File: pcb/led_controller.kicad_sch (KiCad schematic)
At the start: 38 parts, among them IC1 IS31FL3254-QFLS4-TR

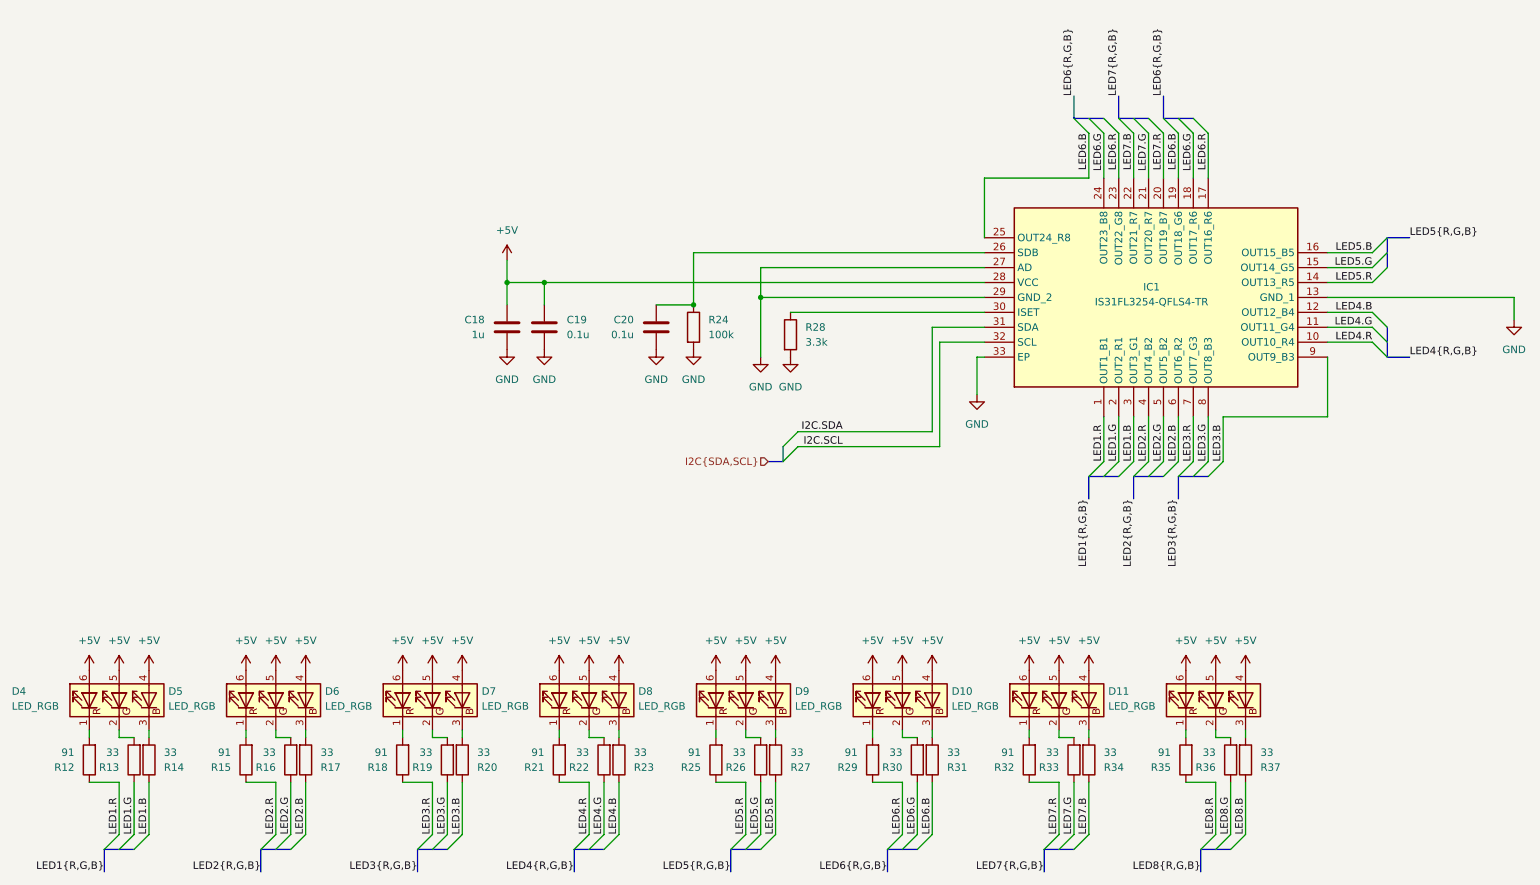
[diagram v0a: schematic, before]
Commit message: redraw led controller ic symbol
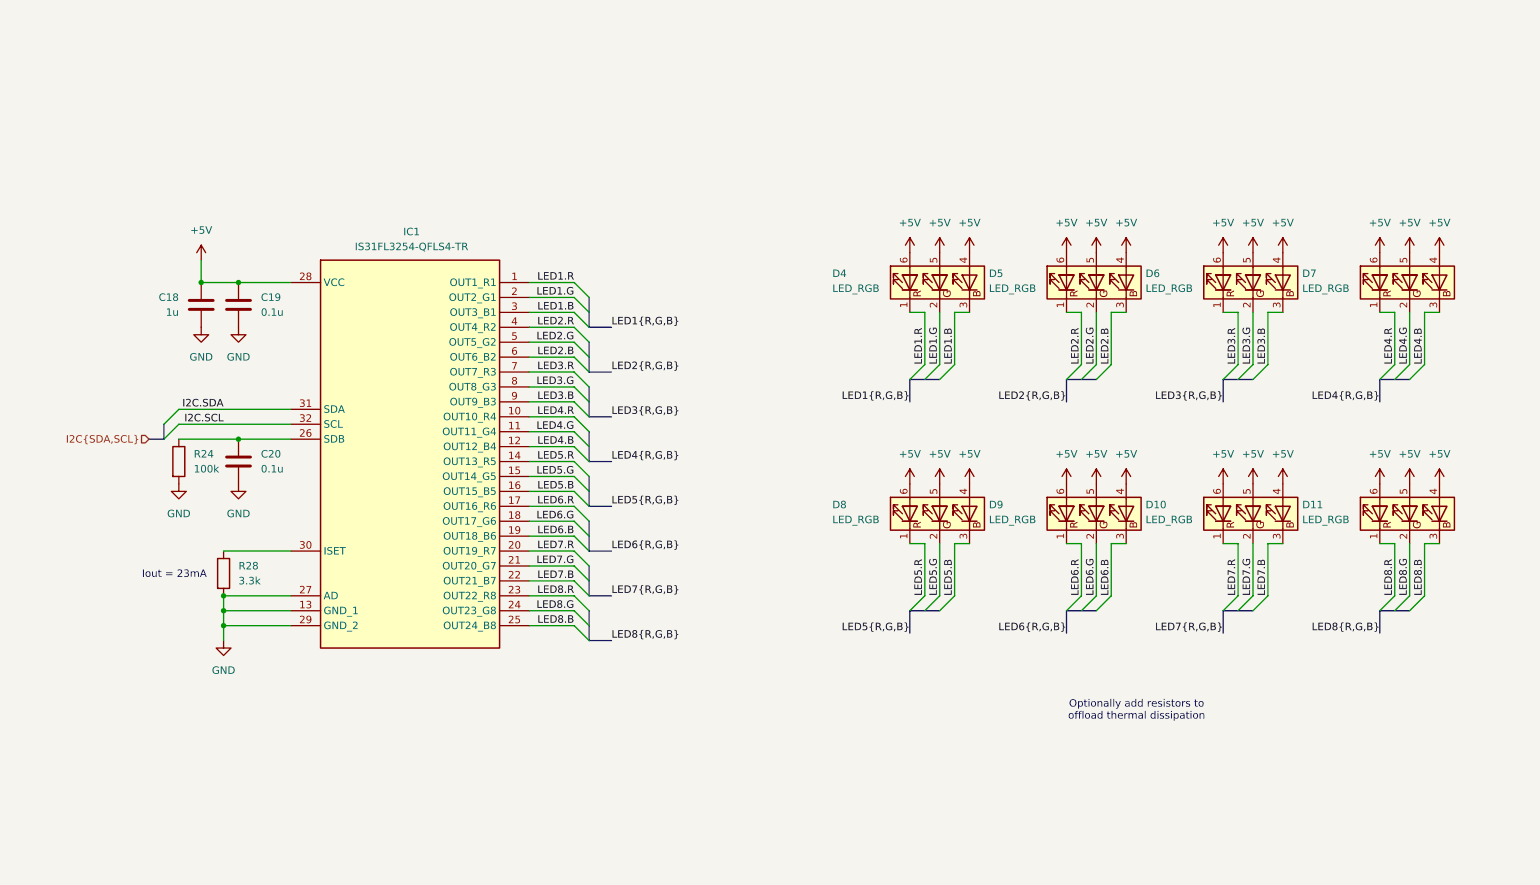
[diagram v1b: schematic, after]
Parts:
- removed R12, R15, R18, R21, R25, R29, R32, R35: 91, Resistor_SMD:R_0402_1005Metric, symbol Device:R
- removed R13, R14, R16, R17, R19, R20, R22, R23, R26, R27, R30, R31, R33, R34, R36, R37: 33, Resistor_SMD:R_0402_1005Metric, symbol Device:R
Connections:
- net GND: no longer IC1.33 (EP)
- net LED1.B: now also D4.3 (BK)
- net LED1.G: now also D4.2 (GK)
- net LED1.R: now also D4.1 (RK)
- net LED2.B: now also D5.3 (BK)
- net LED2.G: now also D5.2 (GK)
- net LED2.R: now also D5.1 (RK)
- net LED3.B: now also D6.3 (BK)
- net LED3.G: now also D6.2 (GK)
- net LED3.R: now also D6.1 (RK)
- net LED4.B: now also D7.3 (BK)
- net LED4.G: now also D7.2 (GK)
- net LED4.R: now also D7.1 (RK)
- net LED5.B: now also D8.3 (BK)
- net LED5.G: now also D8.2 (GK)
- net LED5.R: now also D8.1 (RK)
- net LED6.B: now also D9.3 (BK); no longer IC1.25 (OUT24_R8)
- net LED6.G: now also D9.2 (GK); no longer IC1.24 (OUT23_B8)
- net LED6.R: now also D9.1 (RK); no longer IC1.23 (OUT22_G8)
- net LED7.B: now also D10.3 (BK)
- net LED7.G: now also D10.2 (GK)
- net LED7.R: now also D10.1 (RK)
- net LED8.B: now also D11.3 (BK), IC1.25 (OUT24_B8)
- net LED8.G: now also D11.2 (GK), IC1.24 (OUT23_G8)
- net LED8.R: now also D11.1 (RK), IC1.23 (OUT22_R8)
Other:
- note added: "Iout = 23mA"
- note added: "Optionally add resistors to offload thermal dissipation"
- moved on the sheet: C20, D10, D11, D4, D5, D6, D7, D8, D9, R24

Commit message: cleanup routing
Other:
- note added: "LED Driver"
- note added: "RGB LEDs"
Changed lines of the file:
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@@
 		(title "LED Controller")
 		(date "2026-10-27")
+		(comment 1 "Madison Hua")
+	)
+	(rectangle
+		(start 148.59 44.45)
+		(end 267.97 142.24)
+		(stroke
+			(width 0)
+			(type default)
+		)
+		(fill
+			(type none)
+		)
+	)
+	(rectangle
+		(start 20.32 44.45)
+		(end 135.89 133.35)
+		(stroke
+			(width 0)
+			(type default)
+		)
+		(fill
+			(type none)
+		)
 	)
 	(text "Optionally add resistors to\noffload thermal dissipation"
@@
 		)
 	)
+	(text "LED Driver"
+		(exclude_from_sim no)
+		(at 25.4 42.672 0)
+		(effects
+			(font
+				(size 1.27 1.27)
+			)
+		)
+	)
 	(text ""
 		(exclude_from_sim no)
 		(at 211.074 132.08 0)
+		(effects
+			(font
+				(size 1.27 1.27)
+			)
+		)
+	)
+	(text "RGB LEDs"
+		(exclude_from_sim no)
+		(at 153.162 42.672 0)
 		(effects
 			(font
@@
 	(symbol
 		(lib_id "IS31FL3254-QFLS4-TR:IS31FL3254-QFLS4-TR")
-		(at 63.5 57.15 0)
+		(at 83.82 87.63 0)
 		(unit 1)
 		(body_style 1)
@@
 		)
 		(property "Footprint" "QFN40P400X400X80-33N-D"
-			(at 100.33 139.37 0)
+			(at 70.866 130.48 0)
 			(hide yes)
 			(show_name no)
@@
 		)
 		(property "Datasheet" "https://www.lumissil.com/assets/pdf/core/IS31FL3254_DS.pdf"
-			(at 100.33 239.37 0)
+			(at 120.65 269.85 0)
 			(hide yes)
 			(show_name no)
@@
 		)
 		(property "Description" "24-CHANNEL LED DRIVER, QFN-32, 4mm4mm, T&R"
-			(at 63.5 57.15 0)
+			(at 84.328 127.254 0)
 			(hide yes)
 			(show_name no)
@@
 		)
 		(property "Height" "0.8"
-			(at 100.33 439.37 0)
+			(at 120.65 469.85 0)
 			(hide yes)
 			(show_name no)
@@
 		)
 		(property "Manufacturer_Name" "Lumissil Microsystems"
-			(at 100.33 539.37 0)
+			(at 120.65 569.85 0)
 			(hide yes)
 			(show_name no)
@@
 		)
 		(property "Manufacturer_Part_Number" "IS31FL3254-QFLS4-TR"
-			(at 100.33 639.37 0)
+			(at 120.65 669.85 0)
 			(hide yes)
 			(show_name no)
@@
 		)
 		(property "Mouser Part Number" ""
-			(at 100.33 739.37 0)
+			(at 120.65 769.85 0)
 			(hide yes)
 			(show_name no)
@@
 		)
 		(property "Mouser Price/Stock" ""
-			(at 100.33 839.37 0)
+			(at 120.65 869.85 0)
 			(hide yes)
 			(show_name no)
@@
 		)
 		(property "Arrow Part Number" "IS31FL3254-QFLS4-TR"
-			(at 100.33 939.37 0)
+			(at 120.65 969.85 0)
 			(hide yes)
 			(show_name no)
@@
 		)
 		(property "Arrow Price/Stock" "https://www.arrow.com/en/products/is31fl3254-qfls4-tr/lumissil-microsystems.html?utm_currency=USD&region=nac"
-			(at 100.33 1039.37 0)
-			(hide yes)
-			(show_name no)
+			(at 120.65 1069.85 0)
+			(hide yes)
+			(show_name no)

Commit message: separate peripherals onto different i2c busses
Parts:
- R28: value 3.3k -> 15k
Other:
- note added: "Iout = 5mA"
- note removed: "Iout = 23mA"
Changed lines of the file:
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@@
 		)
 	)
-	(text "Iout = 23mA"
+	(text "Iout = 5mA"
 		(exclude_from_sim no)
 		(at 43.688 110.744 0)
@@
 			)
 		)
-		(property "Value" "3.3k"
+		(property "Value" "15k"
 			(at 54.61 111.7599 0)
 			(show_name no)
